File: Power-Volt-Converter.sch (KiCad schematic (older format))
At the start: 28 parts, among them P22 XT60, P23 XT60, P24 XT60, P25 XT60, P26 XT60, P27 XT60, P28 XT60, P29 XT60, Q15 BC817-40, U1 I6A24014A033V, U10 TEN_20-2411WIN, U11 TEN_20-2411WIN, U7 UWE-12/6-Q12P

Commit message: Update Netlist
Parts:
- C19: renamed from C1; footprint (none) -> Capacitors_SMD:CP_Elec_8x10.5
- R36: renamed from R2; footprint (none) -> Resistors_SMD:R_0603
- R37: renamed from R3; footprint (none) -> Resistors_SMD:R_0603
- U10: renamed from U1; footprint (none) -> zeabus:I6A24014A033V
- renumbered D17 to D13, D20 to D14, D1 to D15, D21 to D16, D2 to D17, P27 to P23, P25 to P24, P26 to P25, P29 to P26, P28 to P27, P23 to P28, P24 to P29, Q15 to Q9, R44 to R32, R46 to R33, R51 to R34, R1 to R35, R52 to R38, R4 to R39, U10 to U8, U11 to U9
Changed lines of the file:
@@
 $EndDescr
 $Comp
-L GND #PWR8
+L GND #PWR53
 U 1 1 58C84F3D
 P 7250 2350
-F 0 "#PWR8" H 7250 2100 60  0001 C CNN
+F 0 "#PWR53" H 7250 2100 60  0001 C CNN
 F 1 "GND" H 7250 2200 60  0000 C CNN
 F 2 "" H 7250 2350 60  0000 C CNN
@@
 $EndComp
 $Comp
-L GND #PWR2
+L GND #PWR47
 U 1 1 58C8506B
 P 2250 1600
-F 0 "#PWR2" H 2250 1350 60  0001 C CNN
+F 0 "#PWR47" H 2250 1350 60  0001 C CNN
 F 1 "GND" H 2250 1450 60  0000 C CNN
 F 2 "" H 2250 1600 60  0000 C CNN
@@
 $EndComp
 $Comp
-L R R46
+L R R33
 U 1 1 58C85083
 P 4000 1650
-F 0 "R46" V 4080 1650 40  0000 C CNN
+F 0 "R33" V 4080 1650 40  0000 C CNN
 F 1 "1k" V 4007 1651 40  0000 C CNN
 F 2 "Resistors_SMD:R_0603" V 3930 1650 30  0001 C CNN
@@
 $EndComp
 $Comp
-L LED_Small D17
+L LED_Small D13
 U 1 1 58C85089
 P 4000 1900
-F 0 "D17" H 3950 2025 50  0000 L CNN
+F 0 "D13" H 3950 2025 50  0000 L CNN
 F 1 "Led_Small" H 3825 1800 50  0000 L CNN
 F 2 "LEDs:LED_0603" V 4000 1900 60  0001 C CNN
@@
 $EndComp
 $Comp
-L R R51
+L R R34
 U 1 1 58C85236
 P 4200 3800
-F 0 "R51" V 4280 3800 40  0000 C CNN
+F 0 "R34" V 4280 3800 40  0000 C CNN
 F 1 "1k" V 4207 3801 40  0000 C CNN
 F 2 "Resistors_SMD:R_0603" V 4130 3800 30  0001 C CNN
@@
 $EndComp
 $Comp
-L LED_Small D20
+L LED_Small D14
 U 1 1 58C8523C
 P 4200 4050
-F 0 "D20" H 4150 4175 50  0000 L CNN
+F 0 "D14" H 4150 4175 50  0000 L CNN
 F 1 "Led_Small" H 4025 3950 50  0000 L CNN
 F 2 "LEDs:LED_0603" V 4200 4050 60  0001 C CNN
@@
 $EndComp
 $Comp
-L XT60 P27
+L XT60 P23
 U 1 1 58C85242
 P 4750 3900
-F 0 "P27" H 4750 4050 50  0000 C CNN
+F 0 "P23" H 4750 4050 50  0000 C CNN
 F 1 "XT60" H 4750 3750 50  0000 C CNN
 F 2 "Zeabus:XT60" H 4750 3900 60  0001 C CNN
@@
 $EndComp
 $Comp
-L GND #PWR5
+L GND #PWR50
 U 1 1 58C8524E
 P 2500 3900
-F 0 "#PWR5" H 2500 3650 60  0001 C CNN
+F 0 "#PWR50" H 2500 3650 60  0001 C CNN
 F 1 "GND" H 2500 3750 60  0000 C CNN
 F 2 "" H 2500 3900 60  0000 C CNN
@@
 $EndComp
 $Comp
-L TEN_20-2411WIN U10
+L TEN_20-2411WIN U8
 U 1 1 58C8526A
 P 3150 3750
-F 0 "U10" H 3150 4187 60  0000 C CNN
+F 0 "U8" H 3150 4187 60  0000 C CNN
 F 1 "TEN_20-2411WIN" H 3150 4081 60  0000 C CNN
 F 2 "Zeabus:TEN_20WIN" H 3200 3650 60  0001 C CNN
@@
 +VBatt
 $Comp
-L +BATT #PWR3
+L +BATT #PWR48
 U 1 1 58C81568
 P 2500 1400
-F 0 "#PWR3" H 2500 1250 50  0001 C CNN
+F 0 "#PWR48" H 2500 1250 50  0001 C CNN
 F 1 "+BATT" H 2500 1540 50  0000 C CNN
 F 2 "" H 2500 1400 50  0000 C CNN
@@
 $EndComp
 $Comp
-L BC817-40 Q15
+L BC817-40 Q9
 U 1 1 58C81AD3
 P 2500 2500
-F 0 "Q15" H 2700 2575 50  0000 L CNN
+F 0 "Q9" H 2700 2575 50  0000 L CNN
 F 1 "BC817-40" H 2700 2500 50  0000 L CNN
 F 2 "TO_SOT_Packages_SMD:SOT-23" H 2700 2425 50  0001 L CIN
@@
 $EndComp
 $Comp
-L GND #PWR6
+L GND #PWR51
 U 1 1 58C8A79D
 P 2600 2700
-F 0 "#PWR6" H 2600 2450 60  0001 C CNN
+F 0 "#PWR51" H 2600 2450 60  0001 C CNN
 F 1 "GND" H 2600 2550 60  0000 C CNN
 F 2 "" H 2600 2700 60  0000 C CNN
@@
 $EndComp
 $Comp
-L R R44
+L R R32
 U 1 1 58C8A817
 P 2250 2300
-F 0 "R44" V 2330 2300 40  0000 C CNN
+F 0 "R32" V 2330 2300 40  0000 C CNN
 F 1 "10k" V 2257 2301 40  0000 C CNN
 F 2 "Resistors_SMD:R_0603" V 2180 2300 30  0001 C CNN
@@
 $EndComp
 $Comp
-L GND #PWR1
+L GND #PWR46
 U 1 1 58C8B273
 P 1450 2700
-F 0 "#PWR1" H 1450 2450 60  0001 C CNN
+F 0 "#PWR46" H 1450 2450 60  0001 C CNN
 F 1 "GND" H 1450 2550 60  0000 C CNN
 F 2 "" H 1450 2700 60  0000 C CNN
@@
 $EndComp
 $Comp
-L XT60 P25
+L XT60 P24
 U 1 1 58C8B481
 P 4950 1750
-F 0 "P25" H 4950 1900 50  0000 C CNN
+F 0 "P24" H 4950 1900 50  0000 C CNN
 F 1 "XT60" H 4950 1600 50  0000 C CNN
 F 2 "Zeabus:XT60" H 4950 1750 60  0001 C CNN
@@
 Master Supply
 $Comp
-L XT60 P26
+L XT60 P25
 U 1 1 58C8BA0B
 P 5400 1750
-F 0 "P26" H 5400 1900 50  0000 C CNN
+F 0 "P25" H 5400 1900 50  0000 C CNN
 F 1 "XT60" H 5400 1600 50  0000 C CNN
 F 2 "Zeabus:XT60" H 5400 1750 60  0001 C CNN
@@
 $EndComp
 $Comp
-L +BATT #PWR4
+L +BATT #PWR49
 U 1 1 58C8C536
 P 2500 3550
-F 0 "#PWR4" H 2500 3400 50  0001 C CNN
+F 0 "#PWR49" H 2500 3400 50  0001 C CNN
 F 1 "+BATT" H 2500 3690 50  0000 C CNN
 F 2 "" H 2500 3550 50  0000 C CNN
@@
 $EndComp
 $Comp
-L +BATT #PWR9
+L +BATT #PWR54
 U 1 1 58C8D087
 P 7350 1650
-F 0 "#PWR9" H 7350 1500 50  0001 C CNN
+F 0 "#PWR54" H 7350 1500 50  0001 C CNN
 F 1 "+BATT" H 7350 1790 50  0000 C CNN
 F 2 "" H 7350 1650 50  0000 C CNN
@@
 Lamp1
 $Comp
-L XT60 P24
+L XT60 P29
 U 1 1 58C8E09C
 P 10850 2050
-F 0 "P24" H 10850 2200 50  0000 C CNN
+F 0 "P29" H 10850 2200 50  0000 C CNN
 F 1 "XT60" H 10850 1900 50  0000 C CNN
 F 2 "Zeabus:XT60" H 10850 2050 60  0001 C CNN
@@
 Eth Switch
 $Comp
-L R R52
+L R R38
 U 1 1 58C90964
 P 9400 5300
-F 0 "R52" V 9480 5300 40  0000 C CNN
+F 0 "R38" V 9480 5300 40  0000 C CNN
 F 1 "1k" V 9407 5301 40  0000 C CNN
 F 2 "Resistors_SMD:R_0603" V 9330 5300 30  0001 C CNN
@@
 $EndComp
 $Comp
-L LED_Small D21
+L LED_Small D16
 U 1 1 58C9096A
 P 9400 5550
-F 0 "D21" H 9350 5675 50  0000 L CNN
+F 0 "D16" H 9350 5675 50  0000 L CNN
 F 1 "Led_Small" H 9225 5450 50  0000 L CNN
 F 2 "LEDs:LED_0603" V 9400 5550 60  0001 C CNN
@@
 $EndComp
 $Comp
-L XT60 P28
+L XT60 P27
 U 1 1 58C90970
 P 9950 5400
-F 0 "P28" H 9950 5550 50  0000 C CNN
+F 0 "P27" H 9950 5550 50  0000 C CNN
 F 1 "XT60" H 9950 5250 50  0000 C CNN
 F 2 "Zeabus:XT60" H 9950 5400 60  0001 C CNN
@@
 $EndComp
 $Comp
-L GND #PWR12
+L GND #PWR57
 U 1 1 58C9097C
 P 7700 5400
-F 0 "#PWR12" H 7700 5150 60  0001 C CNN
+F 0 "#PWR57" H 7700 5150 60  0001 C CNN
 F 1 "GND" H 7700 5250 60  0000 C CNN
 F 2 "" H 7700 5400 60  0000 C CNN
@@
 $EndComp
 $Comp
-L TEN_20-2411WIN U11
+L TEN_20-2411WIN U9
 U 1 1 58C90989
 P 8350 5250
-F 0 "U11" H 8350 5687 60  0000 C CNN
+F 0 "U9" H 8350 5687 60  0000 C CNN
 F 1 "TEN_20-2411WIN" H 8350 5581 60  0000 C CNN
 F 2 "Zeabus:TEN_20WIN" H 8400 5150 60  0001 C CNN
@@
 $EndComp
 $Comp
-L +BATT #PWR11
+L +BATT #PWR56
 U 1 1 58C909A2
 P 7700 5050
-F 0 "#PWR11" H 7700 4900 50  0001 C CNN
+F 0 "#PWR56" H 7700 4900 50  0001 C CNN
 F 1 "+BATT" H 7700 5190 50  0000 C CNN
 F 2 "" H 7700 5050 50  0000 C CNN
@@
 $EndComp
 $Comp
-L GND #PWR13
+L GND #PWR58
 U 1 1 58C909A9
 P 7800 6000
-F 0 "#PWR13" H 7800 5750 60  0001 C CNN
+F 0 "#PWR58" H 7800 5750 60  0001 C CNN
 F 1 "GND" H 7800 5850 60  0000 C CNN
 F 2 "" H 7800 6000 60  0000 C CNN
@@
 USB Hub
 $Comp
-L XT60 P29
+L XT60 P26
 U 1 1 58C90D7F
 P 5400 3900
-F 0 "P29" H 5400 4050 50  0000 C CNN
+F 0 "P26" H 5400 4050 50  0000 C CNN
 F 1 "XT60" H 5400 3750 50  0000 C CNN
 F 2 "Zeabus:XT60" H 5400 3900 60  0001 C CNN
@@
 DSP_Switch_E
 $Comp
-L D_Zener D1
+L D_Zener D15
 U 1 1 58E6F6E6
 P 6700 2000
-F 0 "D1" H 6700 2100 50  0000 C CNN
+F 0 "D15" H 6700 2100 50  0000 C CNN
 F 1 "BZX585-C12" H 6700 1900 50  0000 C CNN
 F 2 "Diodes_SMD:D_SOD-523" H 6700 2000 50  0001 C CNN
@@
 $EndComp
 $Comp
-L R R1
+L R R35
 U 1 1 58E6F94F
 P 6900 1700
-F 0 "R1" V 6980 1700 40  0000 C CNN
+F 0 "R35" V 6980 1700 40  0000 C CNN
 F 1 "10k" V 6907 1701 40  0000 C CNN
 F 2 "Resistors_SMD:R_0603" V 6830 1700 30  0001 C CNN
@@
 $EndComp
 $Comp
-L GND #PWR7
+L GND #PWR52
 U 1 1 58E6FD35
 P 6700 2150
-F 0 "#PWR7" H 6700 1900 60  0001 C CNN
+F 0 "#PWR52" H 6700 1900 60  0001 C CNN
 F 1 "GND" H 6700 2000 60  0000 C CNN
 F 2 "" H 6700 2150 60  0000 C CNN
@@
 $EndComp
 $Comp
-L I6A24014A033V U1
+L I6A24014A033V U10
 U 1 1 58EF79A7
 P 8400 1550
-F 0 "U1" H 7950 450 60  0000 C CNN
+F 0 "U10" H 7950 450 60  0000 C CNN
 F 1 "I6A24014A033V" H 8250 1550 60  0000 C CNN
-F 2 "" H 8400 1550 60  0001 C CNN
+F 2 "zeabus:I6A24014A033V" H 8400 1550 60  0001 C CNN
 F 3 "" H 8400 1550 60  0001 C CNN
 	1    8400 1550
@@
 $EndComp
 $Comp
-L XT60 P23
+L XT60 P28
 U 1 1 58C84F61
 P 10100 2050
-F 0 "P23" H 10100 2200 50  0000 C CNN
+F 0 "P28" H 10100 2200 50  0000 C CNN
 F 1 "XT60" H 10100 1900 50  0000 C CNN
 F 2 "Zeabus:XT60" H 10100 2050 60  0001 C CNN
@@
 $EndComp
 $Comp
-L R R3
+L R R37
 U 1 1 58EFA965
 P 8950 2200
-F 0 "R3" V 9030 2200 50  0000 C CNN
+F 0 "R37" V 9030 2200 50  0000 C CNN
 F 1 "1.4k" V 8950 2200 50  0000 C CNN
-F 2 "" V 8880 2200 50  0001 C CNN
+F 2 "Resistors_SMD:R_0603" V 8880 2200 50  0001 C CNN
 F 3 "" H 8950 2200 50  0001 C CNN
 	1    8950 2200
@@
 $EndComp
 $Comp
-L C C1
+L C C19
 U 1 1 58EFDBF9
 P 7350 2000
-F 0 "C1" H 7375 2100 50  0000 L CNN
+F 0 "C19" H 7375 2100 50  0000 L CNN
 F 1 "100uF" H 7375 1900 50  0000 L CNN
-F 2 "" H 7388 1850 50  0001 C CNN
+F 2 "Capacitors_SMD:CP_Elec_8x10.5" H 7388 1850 50  0001 C CNN
 F 3 "" H 7350 2000 50  0001 C CNN
 	1    7350 2000
@@
 Connection ~ 7350 2300
 $Comp
-L R R4
+L R R39
 U 1 1 58F01219
 P 9450 1950
-F 0 "R4" V 9530 1950 40  0000 C CNN
+F 0 "R39" V 9530 1950 40  0000 C CNN
 F 1 "1k" V 9457 1951 40  0000 C CNN
 F 2 "Resistors_SMD:R_0603" V 9380 1950 30  0001 C CNN
@@
 $EndComp
 $Comp
-L LED_Small D2
+L LED_Small D17
 U 1 1 58F0121F
 P 9450 2200
-F 0 "D2" H 9400 2325 50  0000 L CNN
+F 0 "D17" H 9400 2325 50  0000 L CNN
 F 1 "Led_Small" H 9275 2100 50  0000 L CNN
 F 2 "LEDs:LED_0603" V 9450 2200 60  0001 C CNN
@@
 	7350 1650 7350 1850
 $Comp
-L R R2
+L R R36
 U 1 1 58F08F01
 P 7700 2950
-F 0 "R2" V 7780 2950 50  0000 C CNN
+F 0 "R36" V 7780 2950 50  0000 C CNN
 F 1 "10k" V 7700 2950 50  0000 C CNN
-F 2 "" V 7630 2950 50  0001 C CNN
+F 2 "Resistors_SMD:R_0603" V 7630 2950 50  0001 C CNN
 F 3 "" H 7700 2950 50  0001 C CNN
 	1    7700 2950
@@
 	7700 3100 7700 3200
 $Comp
-L GND #PWR10
+L GND #PWR55
 U 1 1 58F09347
 P 7700 3200
-F 0 "#PWR10" H 7700 2950 60  0001 C CNN
+F 0 "#PWR55" H 7700 2950 60  0001 C CNN
 F 1 "GND" H 7700 3050 60  0000 C CNN
 F 2 "" H 7700 3200 60  0000 C CNN

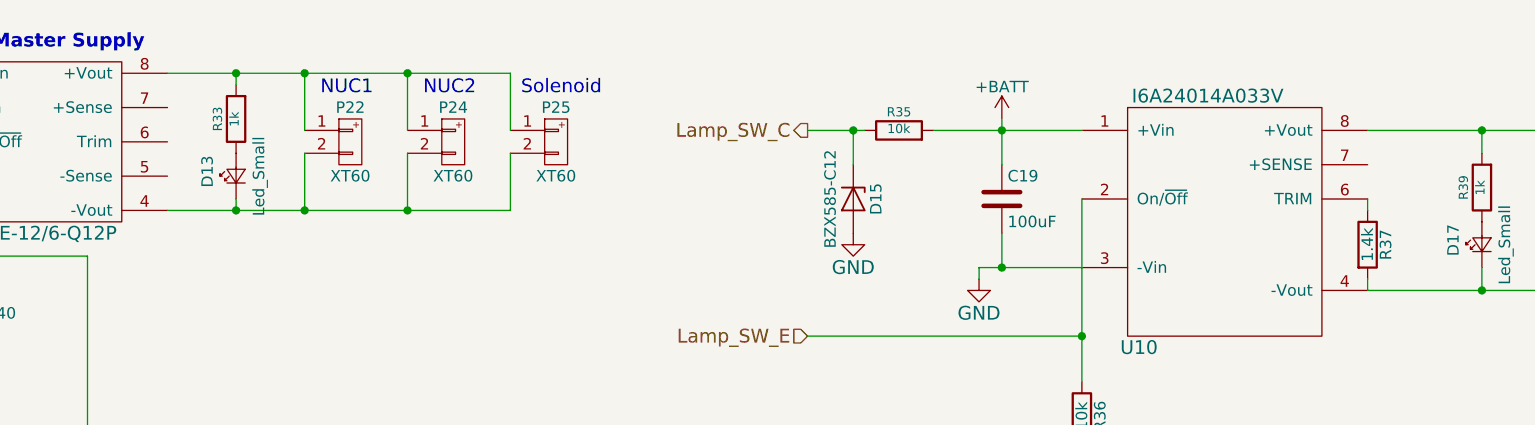
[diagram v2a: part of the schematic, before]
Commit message: Correct GND mixed-up and re-route USB signals as a differential pairs with match length.
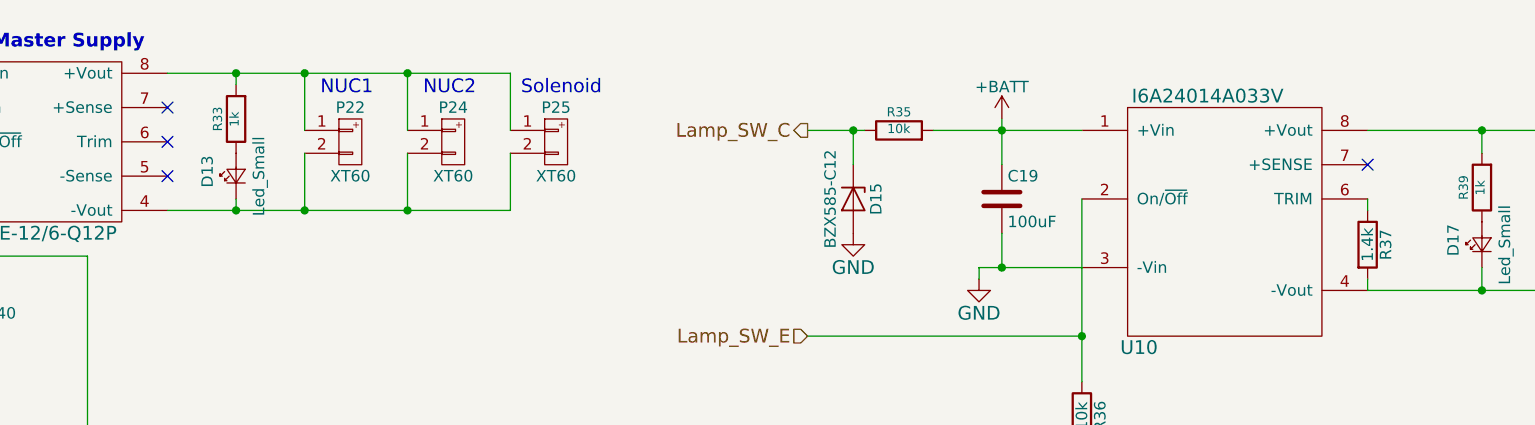
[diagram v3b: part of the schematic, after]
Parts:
- U10: footprint zeabus:I6A24014A033V -> Zeabus:I6A24014A033V
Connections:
- no-connect marks 0 -> 4
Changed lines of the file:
@@
 $Descr A4 11693 8268
 encoding utf-8
-Sheet 10 9
+Sheet 9 9
 Title "Power Voltage Convertor"
 Date "2017-04-06"
@@
 $EndDescr
 $Comp
-L GND #PWR53
+L GND #PWR044
 U 1 1 58C84F3D
 P 7250 2350
-F 0 "#PWR53" H 7250 2100 60  0001 C CNN
+F 0 "#PWR044" H 7250 2100 60  0001 C CNN
 F 1 "GND" H 7250 2200 60  0000 C CNN
 F 2 "" H 7250 2350 60  0000 C CNN
@@
 $EndComp
 $Comp
-L GND #PWR47
+L GND #PWR045
 U 1 1 58C8506B
 P 2250 1600
-F 0 "#PWR47" H 2250 1350 60  0001 C CNN
+F 0 "#PWR045" H 2250 1350 60  0001 C CNN
 F 1 "GND" H 2250 1450 60  0000 C CNN
 F 2 "" H 2250 1600 60  0000 C CNN
@@
 $EndComp
 $Comp
-L GND #PWR50
+L GND #PWR046
 U 1 1 58C8524E
 P 2500 3900
-F 0 "#PWR50" H 2500 3650 60  0001 C CNN
+F 0 "#PWR046" H 2500 3650 60  0001 C CNN
 F 1 "GND" H 2500 3750 60  0000 C CNN
 F 2 "" H 2500 3900 60  0000 C CNN
@@
 +VBatt
 $Comp
-L +BATT #PWR48
+L +BATT #PWR047
 U 1 1 58C81568
 P 2500 1400
-F 0 "#PWR48" H 2500 1250 50  0001 C CNN
+F 0 "#PWR047" H 2500 1250 50  0001 C CNN
 F 1 "+BATT" H 2500 1540 50  0000 C CNN
 F 2 "" H 2500 1400 50  0000 C CNN
@@
 $EndComp
 $Comp
-L GND #PWR51
+L GND #PWR048
 U 1 1 58C8A79D
 P 2600 2700
-F 0 "#PWR51" H 2600 2450 60  0001 C CNN
+F 0 "#PWR048" H 2600 2450 60  0001 C CNN
 F 1 "GND" H 2600 2550 60  0000 C CNN
 F 2 "" H 2600 2700 60  0000 C CNN
@@
 $EndComp
 $Comp
-L GND #PWR46
+L GND #PWR049
 U 1 1 58C8B273
 P 1450 2700
-F 0 "#PWR46" H 1450 2450 60  0001 C CNN
+F 0 "#PWR049" H 1450 2450 60  0001 C CNN
 F 1 "GND" H 1450 2550 60  0000 C CNN
 F 2 "" H 1450 2700 60  0000 C CNN
@@
 $EndComp
 $Comp
-L +BATT #PWR49
+L +BATT #PWR050
 U 1 1 58C8C536
 P 2500 3550
-F 0 "#PWR49" H 2500 3400 50  0001 C CNN
+F 0 "#PWR050" H 2500 3400 50  0001 C CNN
 F 1 "+BATT" H 2500 3690 50  0000 C CNN
 F 2 "" H 2500 3550 50  0000 C CNN
@@
 $EndComp
 $Comp
-L +BATT #PWR54
+L +BATT #PWR051
 U 1 1 58C8D087
 P 7350 1650
-F 0 "#PWR54" H 7350 1500 50  0001 C CNN
+F 0 "#PWR051" H 7350 1500 50  0001 C CNN
 F 1 "+BATT" H 7350 1790 50  0000 C CNN
 F 2 "" H 7350 1650 50  0000 C CNN
@@
 $EndComp
 $Comp
-L GND #PWR57
+L GND #PWR052
 U 1 1 58C9097C
 P 7700 5400
-F 0 "#PWR57" H 7700 5150 60  0001 C CNN
+F 0 "#PWR052" H 7700 5150 60  0001 C CNN
 F 1 "GND" H 7700 5250 60  0000 C CNN
 F 2 "" H 7700 5400 60  0000 C CNN
@@
 $EndComp
 $Comp
-L +BATT #PWR56
+L +BATT #PWR053
 U 1 1 58C909A2
 P 7700 5050
-F 0 "#PWR56" H 7700 4900 50  0001 C CNN
+F 0 "#PWR053" H 7700 4900 50  0001 C CNN
 F 1 "+BATT" H 7700 5190 50  0000 C CNN
 F 2 "" H 7700 5050 50  0000 C CNN
@@
 $EndComp
 $Comp
-L GND #PWR58
+L GND #PWR054
 U 1 1 58C909A9
 P 7800 6000
-F 0 "#PWR58" H 7800 5750 60  0001 C CNN
+F 0 "#PWR054" H 7800 5750 60  0001 C CNN
 F 1 "GND" H 7800 5850 60  0000 C CNN
 F 2 "" H 7800 6000 60  0000 C CNN
@@
 $EndComp
 $Comp
-L GND #PWR52
+L GND #PWR055
 U 1 1 58E6FD35
 P 6700 2150
-F 0 "#PWR52" H 6700 1900 60  0001 C CNN
+F 0 "#PWR055" H 6700 1900 60  0001 C CNN
 F 1 "GND" H 6700 2000 60  0000 C CNN
 F 2 "" H 6700 2150 60  0000 C CNN
@@
 F 0 "U10" H 7950 450 60  0000 C CNN
 F 1 "I6A24014A033V" H 8250 1550 60  0000 C CNN
-F 2 "zeabus:I6A24014A033V" H 8400 1550 60  0001 C CNN
+F 2 "Zeabus:I6A24014A033V" H 8400 1550 60  0001 C CNN
 F 3 "" H 8400 1550 60  0001 C CNN
 	1    8400 1550
@@
 	7700 3100 7700 3200
 $Comp
-L GND #PWR55
+L GND #PWR056
 U 1 1 58F09347
 P 7700 3200
-F 0 "#PWR55" H 7700 2950 60  0001 C CNN
+F 0 "#PWR056" H 7700 2950 60  0001 C CNN
 F 1 "GND" H 7700 3050 60  0000 C CNN
 F 2 "" H 7700 3200 60  0000 C CNN
@@
 	1    0    0    -1
 $EndComp
+NoConn ~ 3700 1600
+NoConn ~ 3700 1750
+NoConn ~ 3700 1900
+NoConn ~ 8950 1850
 $EndSCHEMATC

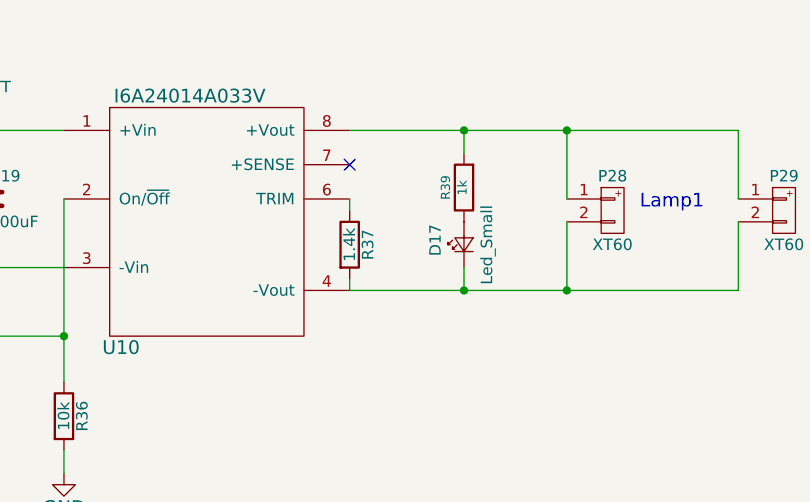
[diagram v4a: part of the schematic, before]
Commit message: change some R value in power circuit to proper value
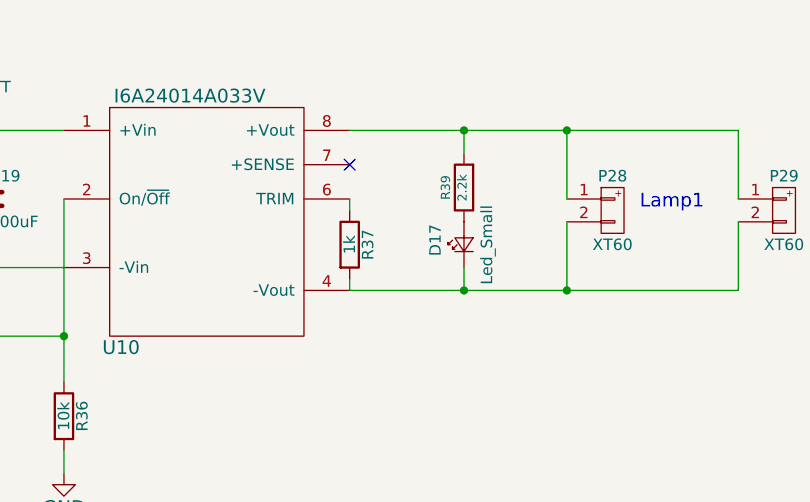
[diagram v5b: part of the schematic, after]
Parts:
- R37: value 1.4k -> 1k
- R39: value 1k -> 2.2k
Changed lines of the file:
@@
 P 8950 2200
 F 0 "R37" V 9030 2200 50  0000 C CNN
-F 1 "1.4k" V 8950 2200 50  0000 C CNN
+F 1 "1k" V 8950 2200 50  0000 C CNN
 F 2 "Resistors_SMD:R_0603" V 8880 2200 50  0001 C CNN
 F 3 "" H 8950 2200 50  0001 C CNN
@@
 P 9450 1950
 F 0 "R39" V 9530 1950 40  0000 C CNN
-F 1 "1k" V 9457 1951 40  0000 C CNN
+F 1 "2.2k" V 9457 1951 40  0000 C CNN
 F 2 "Resistors_SMD:R_0603" V 9380 1950 30  0001 C CNN
 F 3 "" H 9450 1950 30  0000 C CNN

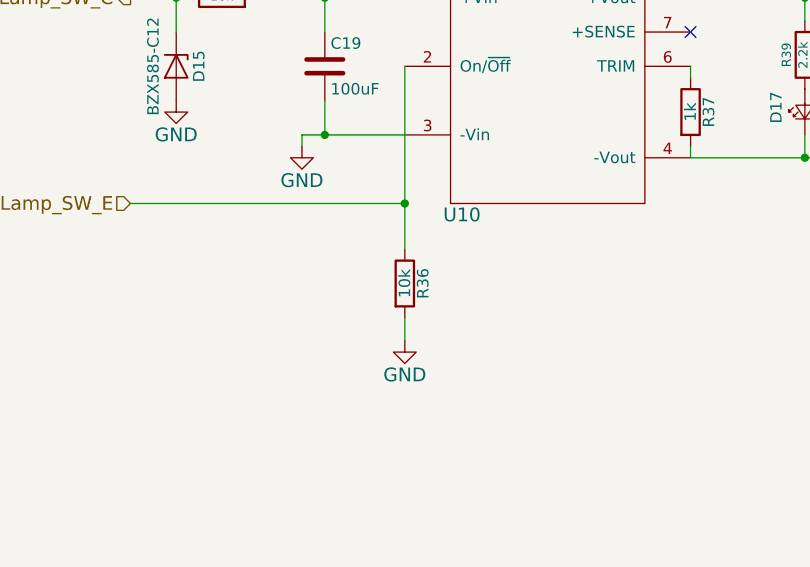
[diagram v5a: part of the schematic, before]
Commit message: change value of R pull down of i6a to 1k ohm
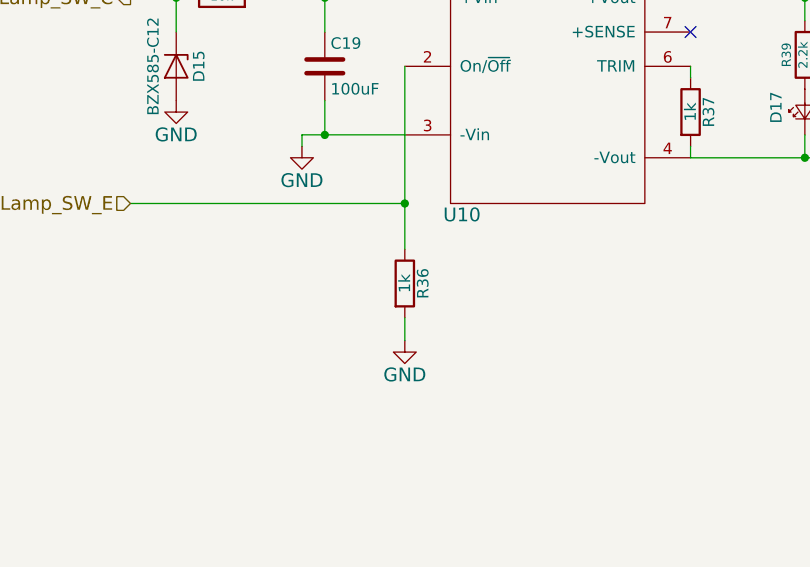
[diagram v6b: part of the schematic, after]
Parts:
- R36: value 10k -> 1k
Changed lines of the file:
@@
 P 7700 2950
 F 0 "R36" V 7780 2950 50  0000 C CNN
-F 1 "10k" V 7700 2950 50  0000 C CNN
+F 1 "1k" V 7700 2950 50  0000 C CNN
 F 2 "Resistors_SMD:R_0603" V 7630 2950 50  0001 C CNN
 F 3 "" H 7700 2950 50  0001 C CNN
